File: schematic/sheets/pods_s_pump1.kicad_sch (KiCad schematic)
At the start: 4 parts, among them U2 DHT22

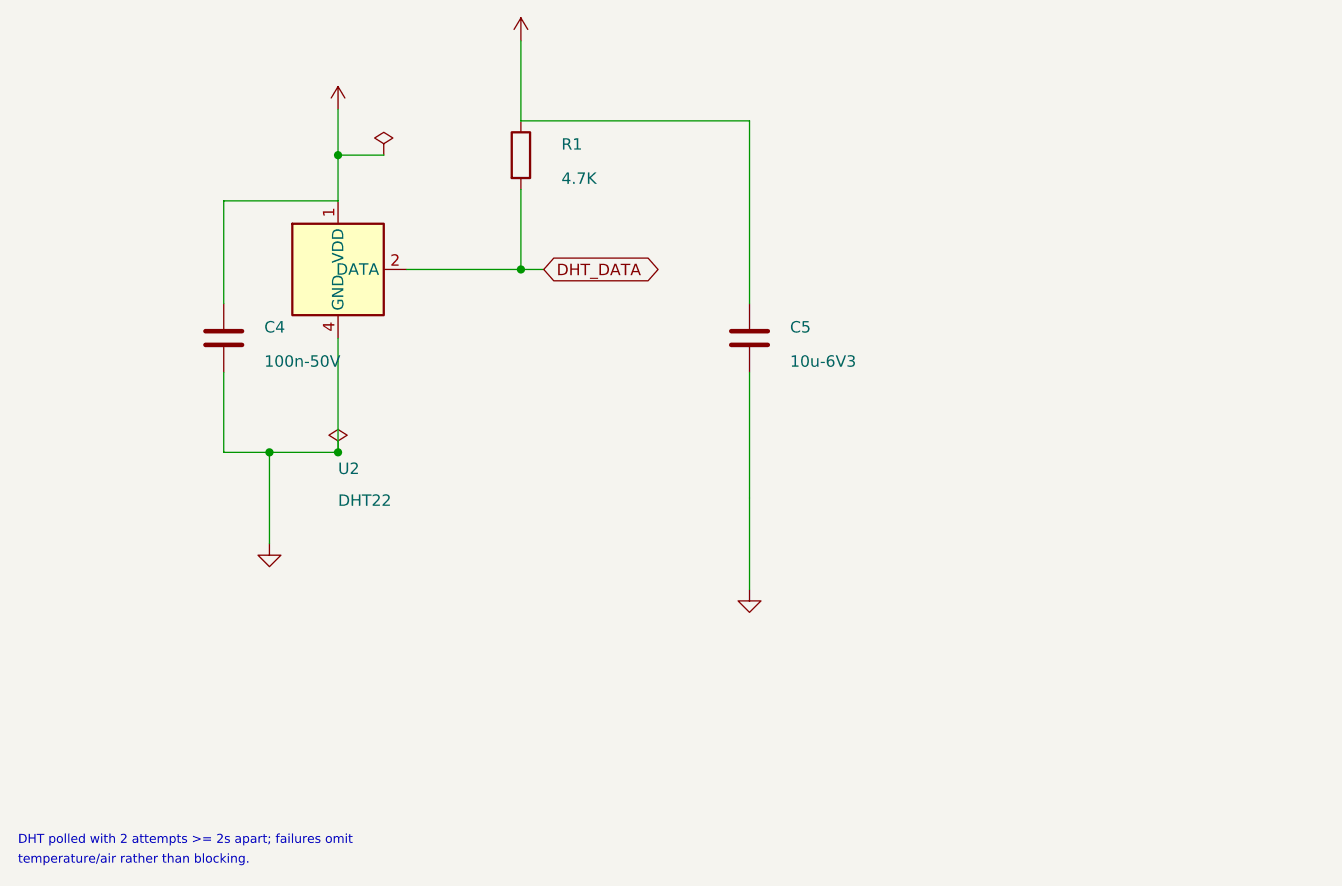
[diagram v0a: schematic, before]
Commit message: Organize schematic/: sheets/ mfg/ final/, drop sklib
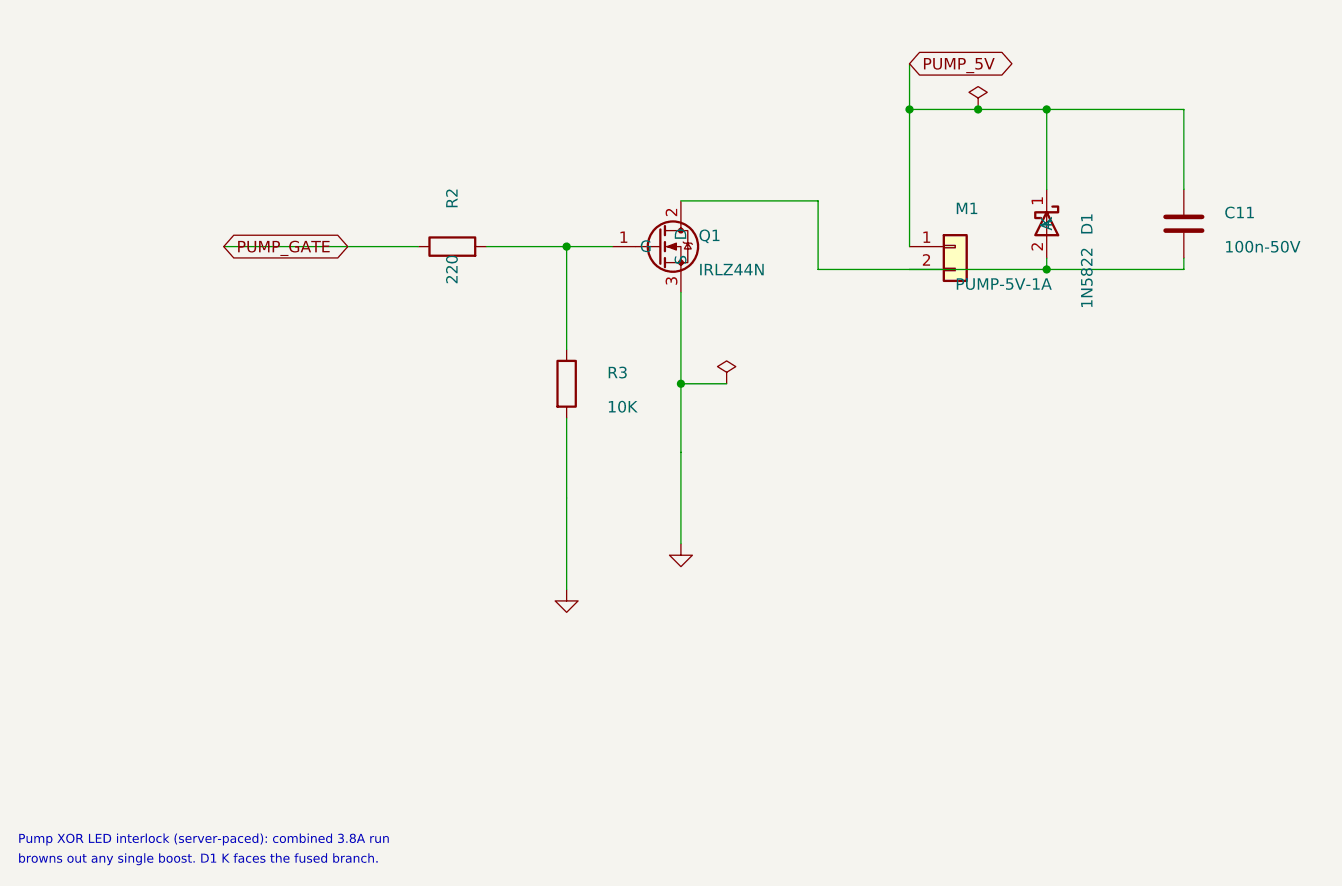
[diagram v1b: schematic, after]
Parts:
- removed C4: 100n-50V, Capacitor_SMD:C_0603_1608Metric, symbol Device:C
- removed C5: 10u-6V3, Capacitor_SMD:C_0603_1608Metric, symbol Device:C
- removed R1: 4.7K, Resistor_SMD:R_0603_1608Metric, symbol Device:R
- removed U2: DHT22, Connector_PinHeader_2.54mm:PinHeader_1x04_P2.54mm_Vertical, symbol Sensor:DHT11
- added C11: 100n-50V, Capacitor_SMD:C_0603_1608Metric, symbol Device:C
- added D1: 1N5822, Diode_THT:D_DO-41_SOD81_P7.62mm_Horizontal, symbol Diode:1N5819
- added M1: PUMP-5V-1A, Connector_PinHeader_2.54mm:PinHeader_1x02_P2.54mm_Vertical, symbol Connector_Generic:Conn_01x02
- added Q1: IRLZ44N, Package_TO_SOT_THT:TO-220-3_Vertical, symbol Transistor_FET:IRLZ44N
- added R2: 220, Resistor_SMD:R_0603_1608Metric, symbol Device:R
- added R3: 10K, Resistor_SMD:R_0603_1608Metric, symbol Device:R
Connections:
- net GND: now also Q1.3 (S), R3.2
- new net: C11.2, D1.2 (A), M1.2 (Pin_2), Q1.2 (D)
- new net: Q1.1 (G), R2.2, R3.1
- new net PUMP_5V: C11.1, D1.1 (K), M1.1 (Pin_1)
- new net PUMP_GATE: R2.1
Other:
- note added: "Pump XOR LED interlock (server-paced): combined 3.8A run"
- note added: "browns out any single boost. D1 K faces the fused branch."
- note removed: "DHT polled with 2 attempts >= 2s apart; failures omit"
- note removed: "temperature/air rather than blocking."
